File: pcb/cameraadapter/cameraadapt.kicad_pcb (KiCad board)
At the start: 4 copper layers, 55.8 x 25 mm, 52 parts, among them J1 Conn_01x30_MountingPin, J2 Conn_01x24_MountingPin, J3 Conn_02x15_Odd_Even_MountingP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, J4 Conn_02x15_Odd_Even_MountingP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, J5 Conn_01x22_MountingPin, J6 Conn_01x22_MountingPin, Q1 DMG1024UV, U1 AP3429K, U3 ADP123, U4 ADP123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

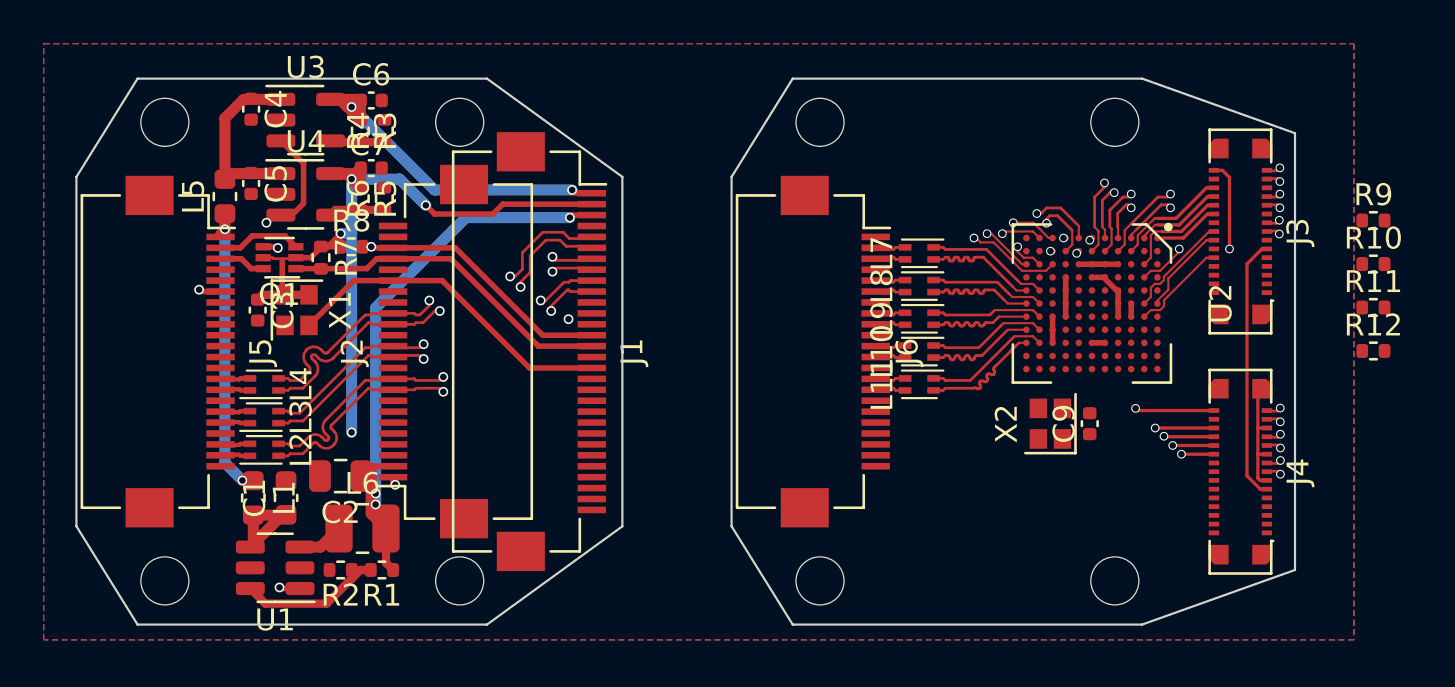
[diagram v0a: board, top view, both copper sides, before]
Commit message: placement verification
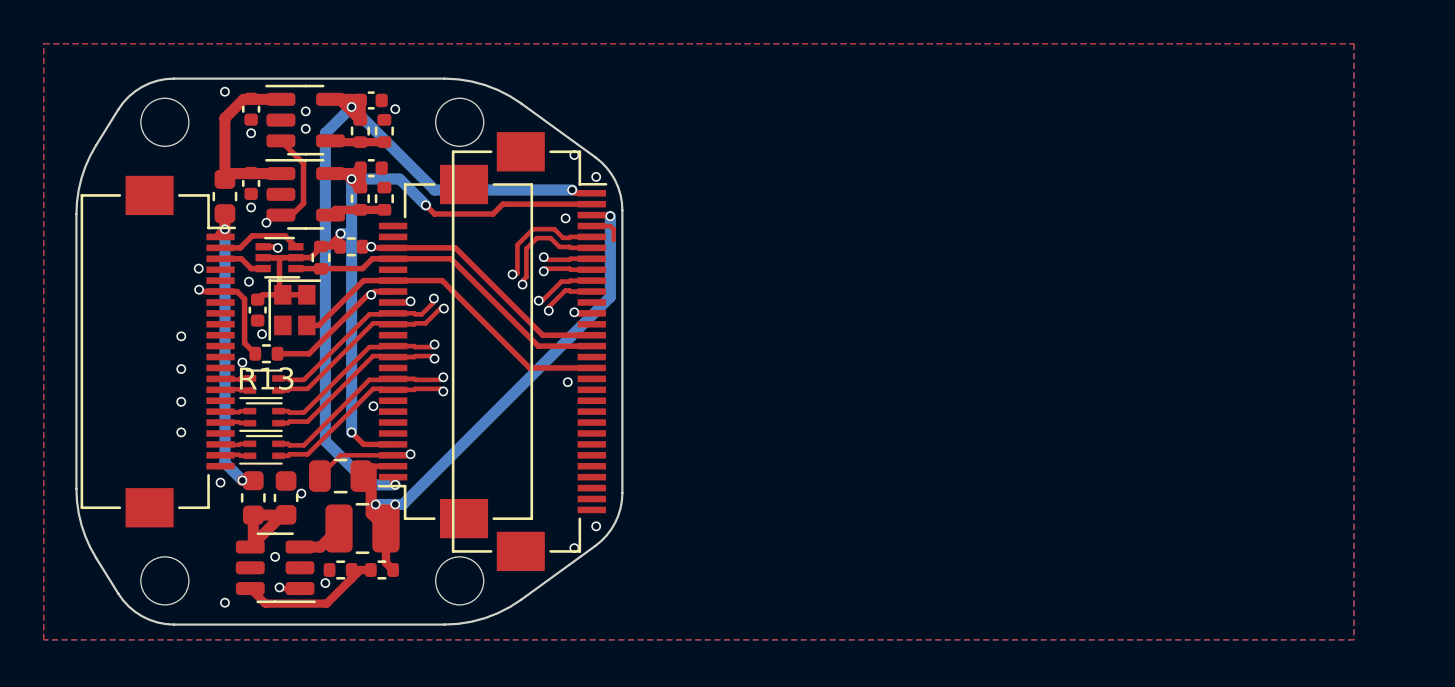
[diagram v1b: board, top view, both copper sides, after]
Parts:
- removed C9: 1u, Capacitor_SMD:C_0402_1005Metric
- removed H5, H6, H7, H8: MountingHole, MountingHole:MountingHole_2.2mm_M2
- removed J3, J4: Conn_02x15_Odd_Even_MountingPin, Connector_Molex:Molex_SlimStack_502426-3010_2x15_P0.40mm_Vertical
- removed J6: Conn_01x22_MountingPin, Connector_FFC-FPC:Hirose_FH12-22S-0.5SH_1x22-1MP_P0.50mm_Horizontal
- removed L10, L11, L7, L8, L9: L_Ferrite_Coupled_Small_1342, Inductor_SMD:L_CommonModeChoke_Coilcraft_0603USB
- removed R10, R11, R12, R9: 2k2, Resistor_SMD:R_0402_1005Metric
- removed U2: ~, Package_BGA:XFBGA-121_8x8mm_Layout11x11_P0.65mm
- removed X2: 27MHz, Crystal:Crystal_SMD_2016-4Pin_2.0x1.6mm
- added R13: 0, Resistor_SMD:R_0402_1005Metric, F.Cu at (-2.10, 0.10)
- moved X1 0.10 mm to (-0.80, -1.90)
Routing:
- net /TOF1_SYNC: track 23.5 -> 0.00 mm, vias 2 -> 0
- net /TOF_RX1_D0_P: track 21.8 -> 0.00 mm, vias 2 -> 0
- net /XSHUTDOWN: track 0.00 -> 21.4 mm, vias 0 -> 2
- net /ERR1_DRV: track 20.9 -> 0.00 mm, vias 2 -> 0
- net /TOF_RX1_D0_N: track 20.7 -> 0.00 mm, vias 2 -> 0
- net /I2C1_SDA: track 19.9 -> 0.00 mm, vias 2 -> 0
- net +2V8: track 17.2 -> 37.0 mm
- net /I2C1_CLK: track 19.7 -> 0.00 mm, vias 2 -> 0
- net /RSTN1_MODULE: track 17.4 -> 0.00 mm, vias 2 -> 0
- net /TOF_RX1_D1_N: track 17.1 -> 0.00 mm, vias 2 -> 0
- net /TOF_RX1_CLK_P: track 16.2 -> 0.00 mm, vias 2 -> 0
- net /TOF_RX1_D1_P: track 15.8 -> 0.00 mm, vias 2 -> 0
- net /EN: track 45.4 -> 30.8 mm, vias 4 -> 3
- net /TOF_RX1_CLK_N: track 14.2 -> 0.00 mm, vias 2 -> 0
- net /TOF_RX0_D1_N: track 12.5 -> 0.00 mm, vias 2 -> 0
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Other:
- board size 55.8 x 25 mm -> 25 x 25 mm
- board text added: "MIPI_CLK matched to p-0.1mm/0.4ps, 22.1047mm MIPI_D1 matched, 22.1057mm MIPI_D0 matched, 22.0958mm use substrate JLC04161H-7628"
